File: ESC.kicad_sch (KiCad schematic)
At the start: 36 parts, among them Q1 SP40N03GNJ, Q2 SP40N03GNJ, Q3 SP40N03GNJ, Q4 SP40N03GNJ, Q5 SP40N03GNJ, Q6 SP40N03GNJ, U2 AT32F421G8U7, U3 NSG2065Q

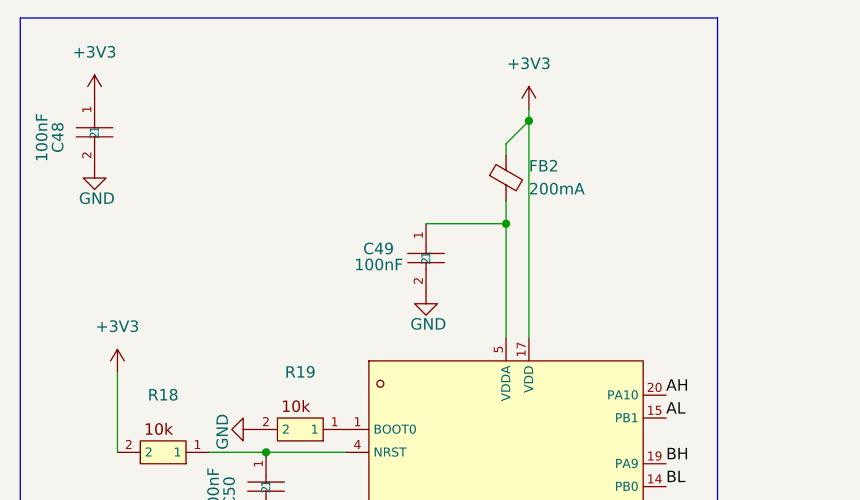
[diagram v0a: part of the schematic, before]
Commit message: Sync v0.4 component changes from 20x20 variant
- INA186A3IDCKR replaces INA199A1DCKR (current sense amp)
- TLV76733DRVR replaces TPS746 (LDO), SNS wired to output
- BLM03PX121SN1D ferrite bead on VDDA
- Add .gitignore for backups and prl files

Co-Authored-By: Claude Opus 4.6 <noreply@anthropic.com>
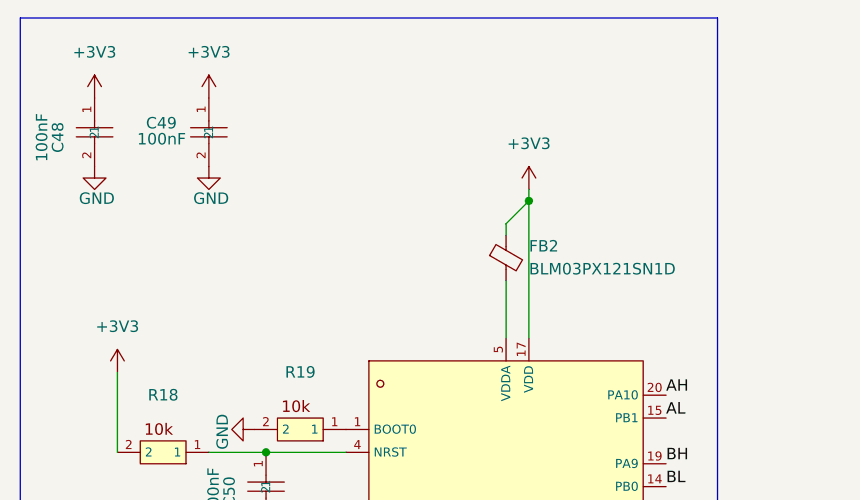
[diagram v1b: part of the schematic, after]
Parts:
- FB2: value 200mA -> BLM03PX121SN1D; LCSC C6132061 -> C525479
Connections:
- net +3V3: now also C49.1
- net at FB2.2, U2.5 (VDDA): no longer C49.1
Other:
- moved on the sheet: C49, FB2
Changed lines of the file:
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@@
 	)
 	(junction
-		(at 74.93 26.67)
+		(at 74.93 35.56)
 		(diameter 0)
 		(color 0 0 0 0)
@@
 	)
 	(junction
-		(at 72.39 38.1)
-		(diameter 0)
-		(color 0 0 0 0)
-	)
-	(junction
 		(at 170.18 73.66)
 		(diameter 0)
@@
 	(wire
 		(pts
-			(xy 72.39 29.21) (xy 74.93 26.67)
+			(xy 72.39 38.1) (xy 74.93 35.56)
 		)
 		(stroke
@@
 	(wire
 		(pts
-			(xy 72.39 35.56) (xy 72.39 38.1)
+			(xy 72.39 44.45) (xy 72.39 50.8)
 		)
 		(stroke
@@
 	(wire
 		(pts
-			(xy 72.39 38.1) (xy 72.39 50.8)
-		)
-		(stroke
-			(width 0)
-			(type default)
-		)
-	)
-	(wire
-		(pts
 			(xy 160.02 73.66) (xy 157.48 73.66)
 		)
@@
 	(wire
 		(pts
-			(xy 74.93 26.67) (xy 74.93 50.8)
+			(xy 74.93 35.56) (xy 74.93 50.8)
 		)
 		(stroke
@@
 	(wire
 		(pts
-			(xy 74.93 25.4) (xy 74.93 26.67)
+			(xy 74.93 34.29) (xy 74.93 35.56)
 		)
 		(stroke
@@
 	(wire
 		(pts
-			(xy 72.39 30.48) (xy 72.39 29.21)
+			(xy 72.39 39.37) (xy 72.39 38.1)
 		)
 		(stroke
@@
 	(wire
 		(pts
-			(xy 63.5 38.1) (xy 72.39 38.1)
-		)
-		(stroke
-			(width 0)
-			(type default)
-		)
-	)
-	(wire
-		(pts
 			(xy 74.93 113.03) (xy 72.39 113.03)
 		)
@@
 	(symbol
 		(lib_id "ESCLibrary:GRM033R61C104KE84D")
-		(at 63.5 41.91 270)
+		(at 39.37 27.94 270)
 		(unit 1)
 		(exclude_from_sim no)
@@
 		(dnp no)
 		(property "Reference" "C49"
-			(at 59.944 40.894 90)
+			(at 35.814 26.924 90)
 			(effects
 				(font
@@
 		)
 		(property "Value" "100nF"
-			(at 60.96 42.672 90)
+			(at 36.83 28.702 90)
 			(effects
 				(font
@@
 		)
 		(property "Footprint" "Capacitor_SMD:C_0201_0603Metric"
-			(at 53.34 41.91 0)
+			(at 29.21 27.94 0)
 			(effects
 				(font
@@
 		)
 		(property "Datasheet" "https://item.szlcsc.com/360022.html"
-			(at 63.627 39.624 0)
+			(at 39.497 25.654 0)
 			(effects
 				(font
@@
 		)
 		(property "Description" ""
-			(at 63.5 41.91 0)
+			(at 39.37 27.94 0)
 			(effects
 				(font
@@
 		)
 		(property "LCSC" "C181043"
-			(at 63.5 41.91 0)
+			(at 39.37 27.94 0)
 			(effects
 				(font
@@
 	)
 	(symbol
+		(lib_id "power:+3V3")
+		(at 39.37 24.13 0)
+		(unit 1)
+		(exclude_from_sim no)
+		(in_bom yes)
+		(on_board yes)
+		(dnp no)
+		(fields_autoplaced yes)
+		(property "Reference" "#PWR067"
+			(at 39.37 27.94 0)
+			(effects
+				(font
+					(size 1.27 1.27)
+				)
+				(hide yes)
+			)
+		)
+		(property "Value" "+3V3"
+			(at 39.37 19.05 0)
+			(effects
+				(font
+					(size 1.27 1.27)
+				)
+			)
+		)
+		(property "Footprint" ""
+			(at 39.37 24.13 0)
+			(effects
+				(font
+					(size 1.27 1.27)
+				)
+				(hide yes)
+			)
+		)
+		(property "Datasheet" ""
+			(at 39.37 24.13 0)
+			(effects
+				(font
+					(size 1.27 1.27)
+				)
+				(hide yes)
+			)
+		)
+		(property "Description" "Power symbol creates a global label with name \"+3V3\""
+			(at 39.37 24.13 0)
+			(effects
+				(font
+					(size 1.27 1.27)
+				)
+				(hide yes)
+			)
+		)
+		(pin "1"
+		)
+		(instances
+			(project "4in1ESC-30x30"
+				(path "/612d09d9-c556-41af-8a15-92be360f8e81/0f1ac7ef-71be-4cf4-81ac-90268323e1b3"
+					(reference "#PWR0110")
+					(unit 1)
+				)
+				(path "/612d09d9-c556-41af-8a15-92be360f8e81/3fa70197-fd52-4922-8368-62c7feb267b9"
+					(reference "#PWR088")
+					(unit 1)
+				)
+				(path "/612d09d9-c556-41af-8a15-92be360f8e81/6061fcc0-8b26-44e0-b078-a202b47fdd16"
+					(reference "#PWR0107")
+					(unit 1)
+				)
+				(path "/612d09d9-c556-41af-8a15-92be360f8e81/f870c78f-43b6-4f66-afe4-21d85c4907b1"
+					(reference "#PWR067")
+					(unit 1)
+				)
+			)
+		)
+	)
+	(symbol
 		(lib_id "ESCLibrary:0201_10kR")
 		(at 254 90.17 270)
@@
 	(symbol
 		(lib_id "power:+3V3")
-		(at 74.93 25.4 0)
+		(at 74.93 34.29 0)
 		(unit 1)
 		(exclude_from_sim no)
@@
 		(fields_autoplaced yes)
 		(property "Reference" "#PWR034"
-			(at 74.93 29.21 0)
+			(at 74.93 38.1 0)
 			(effects
 				(font
@@
 		)
 		(property "Value" "+3V3"
-			(at 74.93 20.32 0)
+			(at 74.93 29.21 0)
 			(effects
 				(font
@@
 		)
 		(property "Footprint" ""
-			(at 74.93 25.4 0)
+			(at 74.93 34.29 0)
 			(effects
 				(font
@@
 		)
 		(property "Datasheet" ""
-			(at 74.93 25.4 0)
+			(at 74.93 34.29 0)
 			(effects
 				(font
@@
 		)
 		(property "Description" "Power symbol creates a global label with name \"+3V3\""
-			(at 74.93 25.4 0)
+			(at 74.93 34.29 0)
 			(effects
 				(font
@@
 	(symbol
 		(lib_id "Device:FerriteBead_Small")
-		(at 72.39 33.02 0)
+		(at 72.39 41.91 0)
 		(unit 1)
 		(exclude_from_sim no)
@@
 		(fields_autoplaced yes)
 		(property "Reference" "FB2"
-			(at 74.93 31.7118 0)
+			(at 74.93 40.6018 0)
 			(effects
 				(font
@@
 			)
 		)
-		(property "Value" "200mA"
-			(at 74.93 34.2518 0)
+		(property "Value" "BLM03PX121SN1D"
+			(at 74.93 43.1418 0)
 			(effects
 				(font
@@
 		)
 		(property "Footprint" "Inductor_SMD:L_0201_0603Metric"
-			(at 70.612 33.02 90)
+			(at 70.612 41.91 90)
 			(effects
 				(font
@@
 		)
 		(property "Datasheet" "~"
-			(at 72.39 33.02 0)
+			(at 72.39 41.91 0)
 			(effects
 				(font
@@
 		)
 		(property "Description" "Ferrite bead, small symbol"
-			(at 72.39 33.02 0)
+			(at 72.39 41.91 0)
 			(effects
 				(font
@@
 			)
 		)
-		(property "LCSC" "C6132061"
-			(at 72.39 33.02 0)
+		(property "LCSC" "C525479"
+			(at 72.39 41.91 0)
 			(effects
 				(font
@@
 	(symbol
 		(lib_id "power:GND")
-		(at 63.5 45.72 0)
+		(at 39.37 31.75 0)
 		(unit 1)
 		(exclude_from_sim no)
@@
 		(dnp no)
 		(property "Reference" "#PWR029"
-			(at 63.5 52.07 0)
+			(at 39.37 38.1 0)
 			(effects
 				(font
@@
 		)
 		(property "Value" "GND"
-			(at 63.754 49.276 0)
+			(at 39.624 35.306 0)
 			(effects
 				(font
@@
 		)
 		(property "Footprint" ""
-			(at 63.5 45.72 0)
+			(at 39.37 31.75 0)
 			(effects
 				(font
@@
 		)
 		(property "Datasheet" ""
-			(at 63.5 45.72 0)
+			(at 39.37 31.75 0)
 			(effects
 				(font
@@
 		)
 		(property "Description" "Power symbol creates a global label with name \"GND\" , ground"
-			(at 63.5 45.72 0)
+			(at 39.37 31.75 0)
 			(effects
 				(font

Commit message: Prepare for open source: PCB layout, new footprints, 3D models, comprehensive gitignore
- Add PCB layout (4-layer, 30x30mm)
- Add SP40N01GHNK MOSFET footprint and 3D model (PDFN-8L 5x6mm)
- Add NSG20652Q gate driver alt footprint and QFN-24 3D model
- Add board outline footprint and SMB connector footprint/3D model
- Update schematic and symbols for NSG20652Q pinout
- Comprehensive .gitignore matching 20x20 variant
- Fix README link to 20x20 repo

Co-Authored-By: Claude Opus 4.6 <noreply@anthropic.com>
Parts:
- removed Q3, Q4, Q5: SP40N03GNJ, components:POWERPAK-1212-8_L3.0-W3.0-P0.65-LS3.3-BL, symbol PCM_Transistor_MOSFET_AKL:2N6660
- removed R17, R21, R22, R24: 15R, Capacitor_SMD:C_0201_0603Metric, symbol PCM_Resistor_AKL:R_0402
- removed U3: NSG2065Q, components:QFN-24_L4.0-W4.0-P0.50-TL-EP2.8, symbol components:NSG2065Q
- added Q11, Q16, Q21: C22385416, 4in1ESC-30x30:PDFN-8L_L6.0-W5.0-P1.27, symbol PCM_Transistor_MOSFET_AKL:2N6660
- added R2, R43, R60, R9: 8R, Capacitor_SMD:C_0201_0603Metric, symbol PCM_Resistor_AKL:R_0402
- added U4: NSG2065Q, 4in1ESC-30x30:QFN-24_L4.0-W4.0-P0.50-TL-EP2.8, symbol components:NSG2065Q
- C32, C36, C48, C49, C50, C53, C57: symbol ESCLibrary:GRM033R61C104KE84D -> components:GRM033R61C104KE84D
- Q1, Q2, Q6: value SP40N03GNJ -> C22385416; footprint components:POWERPAK-1212-8_L3.0-W3.0-P0.65-LS3.3-BL -> 4in1ESC-30x30:PDFN-8L_L6.0-W5.0-P1.27; LCSC C22466709 -> SP40N01GHNK
- R16, R23: value 15R -> 8R
- R18, R19, R25, R27, R28, R30, R31, R33: symbol ESCLibrary:0201_10kR -> components:0201_10kR
- R20: symbol ESCLibrary:0201_220R -> components:0201_220R
- R26, R29, R32: symbol ESCLibrary:0201_1kR -> components:0201_1kR
- U2: footprint ESCLibrary:QFN-28_L4.0-W4.0-P0.40-TL-EP2.4 -> 4in1ESC-30x30:QFN-28_L4.0-W4.0-P0.40-TL-EP2.4; symbol ESCLibrary:AT32F421G8U7 -> components:AT32F421G8U7
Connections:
- net +8V: now also U4.4 (VCC)
- net +BATT: now also Q6.3 (D), Q16.3 (D)
- net A: now also U4.18 (VS1)
- net AH: now also U4.22 (HIN1)
- net AL: now also U4.1 (LIN1)
- net B: now also Q6.1 (S), Q11.3 (D), U4.15 (VS2)
- net BH: now also U4.23 (HIN2)
- net BL: now also U4.2 (LIN2)
- net C: now also Q16.1 (S), Q21.3 (D), U4.12 (VS3); no longer Q6.3 (D)
- net CH: now also U4.24 (HIN3)
- net CL: now also U4.3 (LIN3)
- net GHA: now also U4.19 (HO1)
- net GHB: now also R9.1, U4.16 (HO2)
- net GHC: now also R43.1, U4.13 (HO3); no longer R23.1
- net GLA: now also R2.1, U4.11 (LO1)
- net GLB: now also R23.1, U4.10 (LO2)
- net GLC: now also R60.1, U4.9 (LO3)
- net GND: now also Q11.1 (S), Q21.1 (S), U4.25 (COM), U4.6 (COM); no longer Q6.1 (S)
- net at C32.2: now also U4.17 (VB2)
- net at C36.2: now also U4.14 (VB3)
- net at C53.2: now also U4.20 (VB1)
- net at Q6.2 (G): now also R9.2
- net at R23.2: now also Q11.2 (G)
- net at Q2.2 (G): now also R2.2
- new net: Q16.2 (G), R43.2
- new net: Q21.2 (G), R60.2
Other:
- moved on the sheet: C32, C36, C53

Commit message: Replace backordered parts with in-stock LCSC alternatives
- 10kΩ 0201: C473048 → C106225 (Yageo, 662k stock)
- Ferrite bead 0201: C525479 → C440127 (330Ω@100MHz, better for VDDA filtering)
- 220Ω 0201: C473535 → C226468 (Yageo)
- 10uF cap: C440198 (0805) → C13585 (1206 basic part, Samsung)
- TVS diode: C908802 → C315992 (Littelfuse SMBJ26A)

Co-Authored-By: Claude Opus 4.6 (1M context) <noreply@anthropic.com>
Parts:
- FB2: LCSC C525479 -> C440127
- R18, R19: LCSC C473048 -> C106225
- R20: LCSC C473535 -> C226468
- TP1, TP4: now left out of the parts list
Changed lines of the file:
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@@
 		(unit 1)
 		(exclude_from_sim no)
-		(in_bom yes)
+		(in_bom no)
 		(on_board yes)
 		(dnp no)
@@
 			)
 		)
-		(property "LCSC" "C473048"
+		(property "LCSC" "C106225"
 			(at 49.53 60.96 0)
 			(effects
@@
 			)
 		)
-		(property "LCSC" "C525479"
+		(property "LCSC" "C440127"
 			(at 72.39 41.91 0)
 			(effects
@@
 			)
 		)
-		(property "LCSC" "C473535"
+		(property "LCSC" "C226468"
 			(at 49.53 80.01 0)
 			(effects
@@
 		(unit 1)
 		(exclude_from_sim no)
-		(in_bom yes)
+		(in_bom no)
 		(on_board yes)
 		(dnp no)
@@
 			)
 		)
-		(property "LCSC" "C473048"
+		(property "LCSC" "C106225"
 			(at 34.29 63.5 0)
 			(effects

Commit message: Standardize repo: .gitignore, README, license, remove production from tracking
- Standardize .gitignore to match ecosystem template
- Update README: simplify license section, remove stale status checklist
- Replace LICENSE stub with full CERN-OHL-S-2.0 text
- Remove production/ from git tracking (generated, re-exportable)
- Add previously untracked licensing/ directory
- Delete empty nextpcb/ directory

Co-Authored-By: Claude Opus 4.6 (1M context) <noreply@anthropic.com>
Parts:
- R25, R27, R28, R30, R31, R33: LCSC C473048 -> C106225
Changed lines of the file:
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@@
 			)
 		)
-		(property "LCSC" "C473048"
+		(property "LCSC" "C106225"
 			(at 234.95 99.06 0)
 			(effects
@@
 			)
 		)
-		(property "LCSC" "C473048"
+		(property "LCSC" "C106225"
 			(at 205.74 90.17 0)
 			(effects
@@
 			)
 		)
-		(property "LCSC" "C473048"
+		(property "LCSC" "C106225"
 			(at 210.82 99.06 0)
 			(effects
@@
 			)
 		)
-		(property "LCSC" "C473048"
+		(property "LCSC" "C106225"
 			(at 259.08 99.06 0)
 			(effects
@@
 			)
 		)
-		(property "LCSC" "C473048"
+		(property "LCSC" "C106225"
 			(at 254 90.17 0)
 			(effects
@@
 			)
 		)
-		(property "LCSC" "C473048"
+		(property "LCSC" "C106225"
 			(at 229.87 90.17 0)
 			(effects
